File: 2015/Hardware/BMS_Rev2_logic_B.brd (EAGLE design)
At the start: 45.4 x 57.3 mm, 38 parts, among them Q9 MOSFET-NCHANNEL2N7002PW

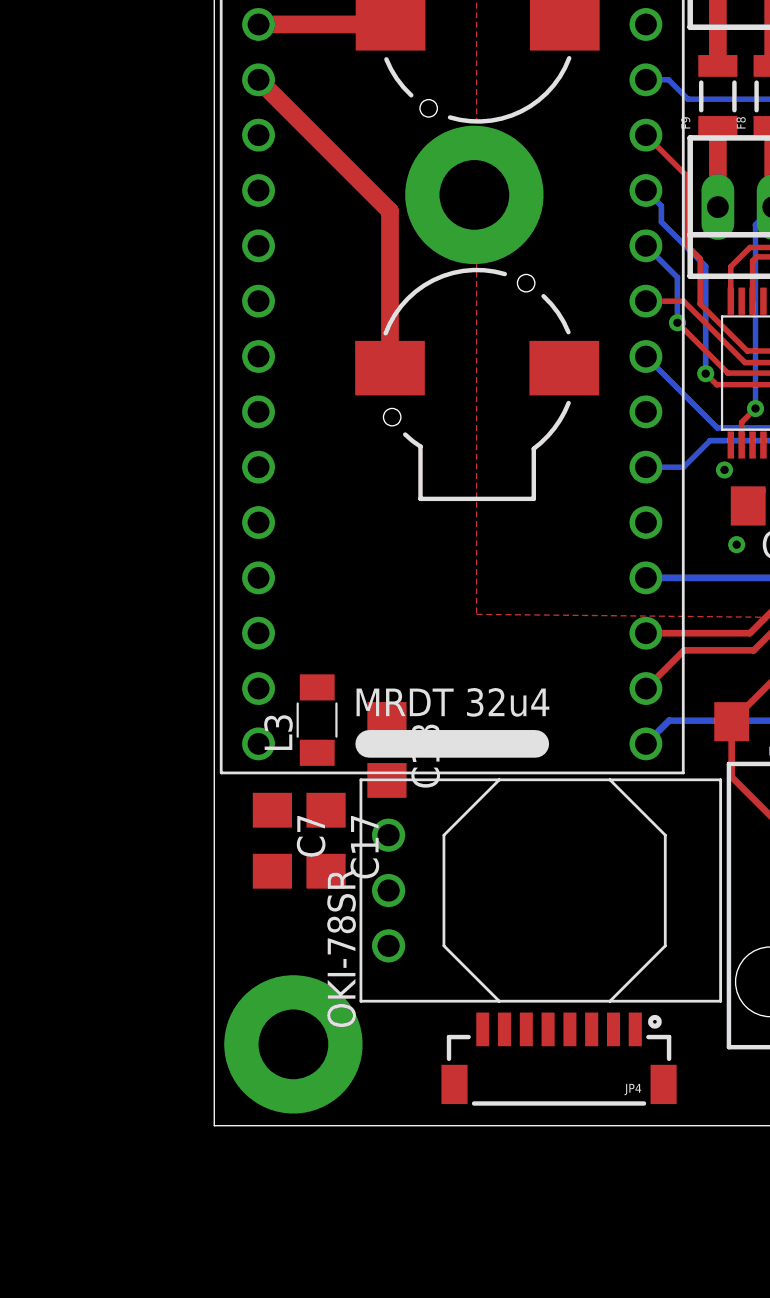
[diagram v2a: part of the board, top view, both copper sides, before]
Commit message: Completed the routing. Needs DRC Check and Clearance adjustments on the polygons
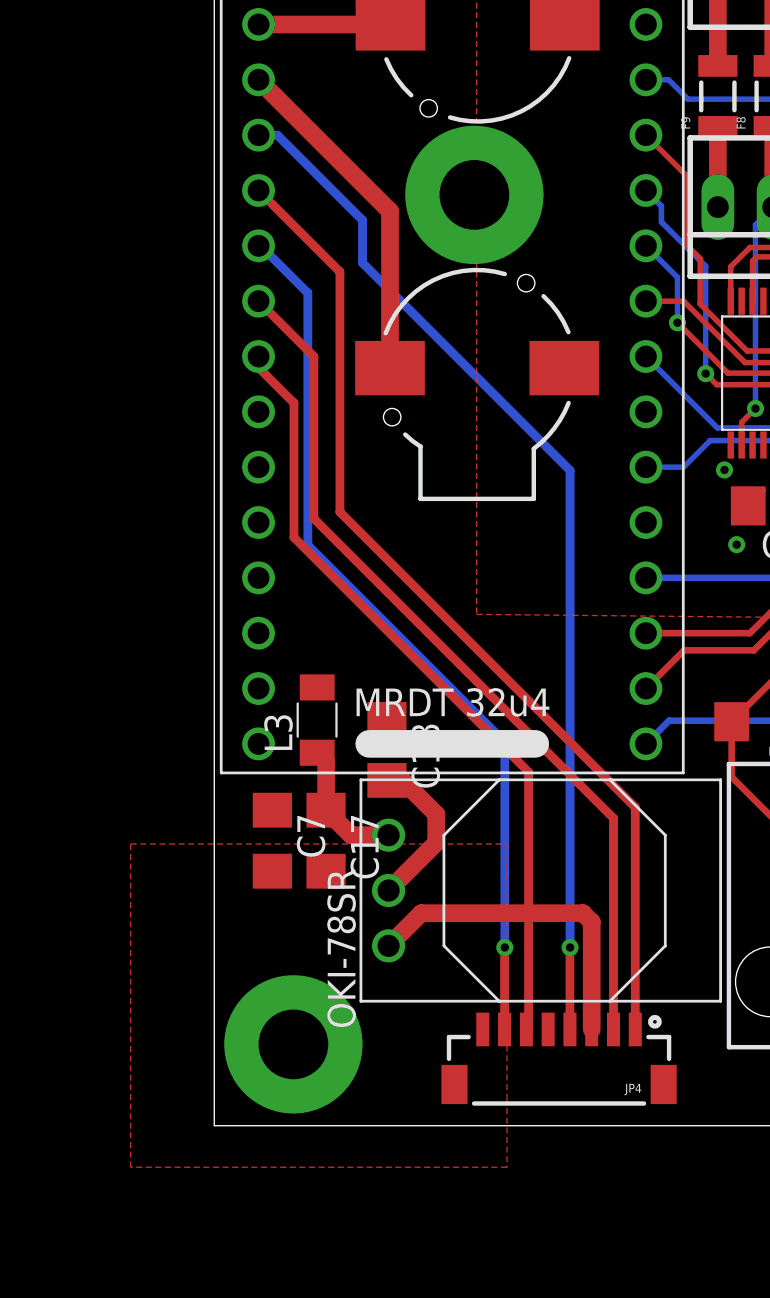
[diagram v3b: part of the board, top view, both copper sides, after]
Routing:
- net V_CHECK: track 0.00 -> 47.5 mm, vias 0 -> 1
- net V_CHG: track 0.00 -> 45.7 mm
- net V_OUT: track 0.00 -> 40.7 mm, vias 0 -> 1
- net I_ARRAY: track 0.00 -> 40.2 mm
- net GATE: track 0.00 -> 36.1 mm
- net LOGIC_POWER: track 0.00 -> 15.0 mm
- net GND: track 23.7 -> 31.0 mm
- net N$100: track 0.00 -> 6.15 mm
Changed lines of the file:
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@@
 <contactref element="S2" pad="P1"/>
 <contactref element="S3" pad="P1"/>
+<polygon width="0.8128" layer="1">
+<vertex x="-3.8354" y="9.6266"/>
+<vertex x="13.4366" y="9.6266"/>
+<vertex x="13.4366" y="-2.0574"/>
+<vertex x="13.4366" y="-5.207"/>
+<vertex x="-3.8354" y="-5.207"/>
+</polygon>
+<wire x1="7.9248" y1="12.5446" x2="8.639" y2="12.5446" width="0.8128" layer="1"/>
+<wire x1="8.639" y1="12.5446" x2="10.1854" y2="10.9982" width="0.8128" layer="1"/>
+<wire x1="10.1854" y1="10.9982" x2="10.1854" y2="9.6774" width="0.8128" layer="1"/>
+<wire x1="10.1854" y1="9.6774" x2="8.001" y2="7.493" width="0.8128" layer="1"/>
 <wire x1="25.206" y1="25.844" x2="25.206" y2="27.942" width="0" layer="19" extent="1-1"/>
-<wire x1="5.1308" y1="8.379" x2="8.001" y2="7.493" width="0" layer="19" extent="1-1"/>
-<wire x1="2.667" y1="8.379" x2="5.1308" y2="8.379" width="0" layer="19" extent="1-1"/>
-<wire x1="7.9248" y1="12.5446" x2="5.1308" y2="8.379" width="0" layer="19" extent="1-1"/>
-<wire x1="12.3242" y1="1.1176" x2="8.001" y2="7.493" width="0" layer="19" extent="1-1"/>
 </signal>
 <signal name="GATE">
 <contactref element="U$3" pad="25"/>
 <contactref element="JP4" pad="6"/>
-<wire x1="14.3242" y1="1.1176" x2="2.032" y2="32.004" width="0" layer="19" extent="1-1"/>
+<wire x1="14.3242" y1="1.1176" x2="14.4272" y2="1.2206" width="0.4064" layer="1"/>
+<wire x1="14.4272" y1="1.2206" x2="14.4272" y2="12.9286" width="0.4064" layer="1"/>
+<wire x1="14.4272" y1="12.9286" x2="3.6576" y2="23.6982" width="0.4064" layer="1"/>
+<wire x1="3.6576" y1="23.6982" x2="3.6576" y2="29.8704" width="0.4064" layer="1"/>
+<wire x1="3.6576" y1="29.8704" x2="2.032" y2="31.496" width="0.4064" layer="1"/>
+<wire x1="2.032" y1="31.496" x2="2.032" y2="32.004" width="0.4064" layer="1"/>
 </signal>
 <signal name="I_ARRAY">
 <contactref element="U$3" pad="24"/>
 <contactref element="JP4" pad="2"/>
-<wire x1="18.3242" y1="1.1176" x2="2.032" y2="34.544" width="0" layer="19" extent="1-1"/>
+<wire x1="18.3242" y1="1.1176" x2="18.3242" y2="10.8096" width="0.4064" layer="1"/>
+<wire x1="18.3242" y1="10.8096" x2="4.572" y2="24.5618" width="0.4064" layer="1"/>
+<wire x1="4.572" y1="24.5618" x2="4.572" y2="32.004" width="0.4064" layer="1"/>
+<wire x1="4.572" y1="32.004" x2="2.032" y2="34.544" width="0.4064" layer="1"/>
 </signal>
 <signal name="SDA">
@@
 <contactref element="L3" pad="1"/>
 <contactref element="OKI-78SR" pad="3"/>
-<wire x1="4.7244" y1="13.8162" x2="5.1308" y2="11.179" width="0" layer="19" extent="1-1"/>
-<wire x1="8.001" y1="10.033" x2="5.1308" y2="11.179" width="0" layer="19" extent="1-1"/>
+<wire x1="5.1308" y1="11.179" x2="5.1308" y2="13.4098" width="0.8128" layer="1"/>
+<wire x1="5.1308" y1="13.4098" x2="4.7244" y2="13.8162" width="0.8128" layer="1"/>
+<wire x1="8.001" y1="10.033" x2="6.2768" y2="10.033" width="0.8128" layer="1"/>
+<wire x1="6.2768" y1="10.033" x2="5.1308" y2="11.179" width="0.8128" layer="1"/>
 </signal>
 <signal name="RXD">
@@
 <contactref element="JP4" pad="7"/>
 <contactref element="U$3" pad="23"/>
-<wire x1="13.3242" y1="1.1176" x2="2.032" y2="37.084" width="0" layer="19" extent="1-1"/>
+<wire x1="2.032" y1="37.084" x2="2.1336" y2="37.084" width="0.4064" layer="16"/>
+<wire x1="2.1336" y1="37.084" x2="4.2926" y2="34.925" width="0.4064" layer="16"/>
+<wire x1="4.2926" y1="34.925" x2="4.2926" y2="23.3426" width="0.4064" layer="16"/>
+<wire x1="4.2926" y1="23.3426" x2="13.335" y2="14.3002" width="0.4064" layer="16"/>
+<wire x1="13.335" y1="14.3002" x2="13.335" y2="4.8768" width="0.4064" layer="16"/>
+<via x="13.335" y="4.8768" extent="1-16" drill="0.381"/>
+<wire x1="13.335" y1="4.8768" x2="13.3242" y2="4.866" width="0.4064" layer="1"/>
+<wire x1="13.3242" y1="4.866" x2="13.3242" y2="1.1176" width="0.4064" layer="1"/>
 </signal>
 <signal name="V_CHECK">
 <contactref element="JP4" pad="4"/>
 <contactref element="U$3" pad="21"/>
-<wire x1="16.3242" y1="1.1176" x2="2.032" y2="42.164" width="0" layer="19" extent="1-1"/>
+<wire x1="2.032" y1="42.164" x2="2.8956" y2="42.164" width="0.4064" layer="16"/>
+<wire x1="2.8956" y1="42.164" x2="6.8072" y2="38.2524" width="0.4064" layer="16"/>
+<wire x1="6.8072" y1="38.2524" x2="6.8072" y2="36.2966" width="0.4064" layer="16"/>
+<wire x1="6.8072" y1="36.2966" x2="16.3322" y2="26.7716" width="0.4064" layer="16"/>
+<wire x1="16.3322" y1="26.7716" x2="16.3322" y2="4.8768" width="0.4064" layer="16"/>
+<via x="16.3322" y="4.8768" extent="1-16" drill="0.381"/>
+<wire x1="16.3322" y1="4.8768" x2="16.3242" y2="4.8688" width="0.4064" layer="1"/>
+<wire x1="16.3242" y1="4.8688" x2="16.3242" y2="1.1176" width="0.4064" layer="1"/>
 </signal>
 <signal name="V_CHG">
 <contactref element="JP4" pad="1"/>
 <contactref element="U$3" pad="22"/>
-<wire x1="19.3242" y1="1.1176" x2="2.032" y2="39.624" width="0" layer="19" extent="1-1"/>
+<wire x1="19.3242" y1="1.1176" x2="19.3242" y2="11.3082" width="0.4064" layer="1"/>
+<wire x1="19.3242" y1="11.3082" x2="5.7658" y2="24.8666" width="0.4064" layer="1"/>
+<wire x1="5.7658" y1="24.8666" x2="5.7658" y2="35.8902" width="0.4064" layer="1"/>
+<wire x1="5.7658" y1="35.8902" x2="2.032" y2="39.624" width="0.4064" layer="1"/>
 </signal>
 <signal name="LOGIC_POWER">
 <contactref element="JP4" pad="3"/>
 <contactref element="OKI-78SR" pad="1"/>
-<wire x1="8.001" y1="4.953" x2="17.3242" y2="1.1176" width="0" layer="19" extent="1-1"/>
+<wire x1="17.3242" y1="1.1176" x2="17.3242" y2="6.0438" width="0.8128" layer="1"/>
+<wire x1="17.3242" y1="6.0438" x2="16.9164" y2="6.4516" width="0.8128" layer="1"/>
+<wire x1="16.9164" y1="6.4516" x2="9.4996" y2="6.4516" width="0.8128" layer="1"/>
+<wire x1="9.4996" y1="6.4516" x2="8.001" y2="4.953" width="0.8128" layer="1"/>
 </signal>
 <signal name="N$4">

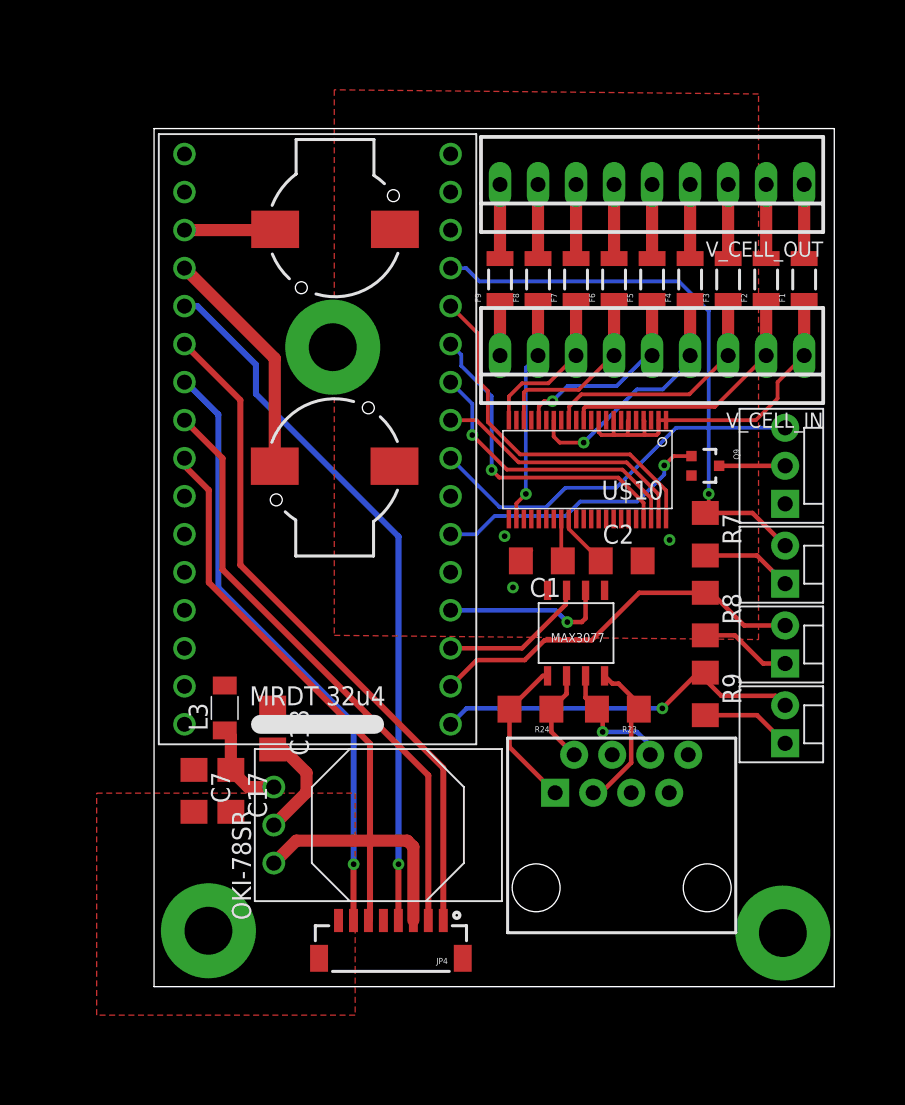
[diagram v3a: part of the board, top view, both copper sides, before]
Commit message: Added Polygons and cleaned up traces. Still clearancework  needs to be done.
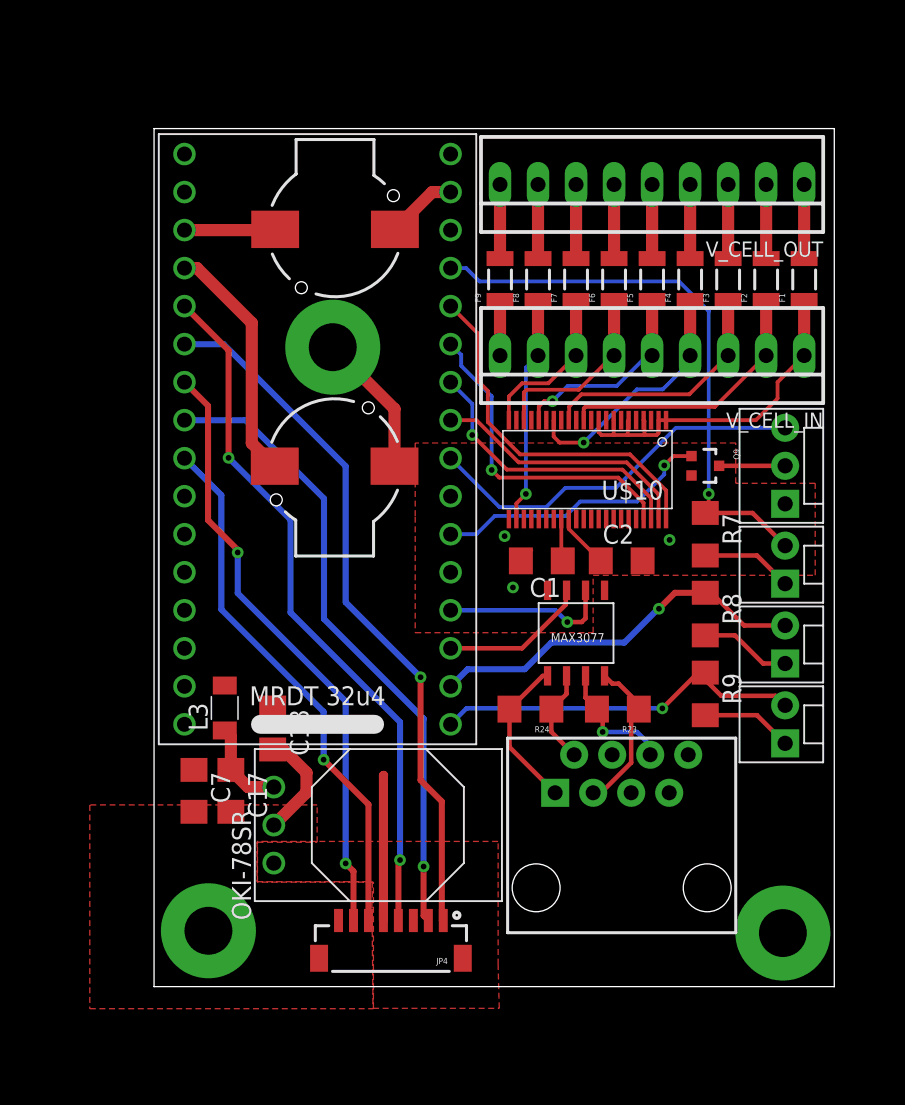
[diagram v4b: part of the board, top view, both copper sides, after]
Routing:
- net LOGIC_POWER: track 15.0 -> 0.00 mm
- net GND: track 31.0 -> 45.4 mm
- net 5V: track 0.00 -> 9.71 mm
- net I_ARRAY: track 40.2 -> 42.6 mm, vias 0 -> 1
- net V_CHG: track 45.7 -> 47.3 mm, vias 0 -> 1
- net V_CHECK: track 47.5 -> 47.1 mm, vias 1 -> 2
- net GATE: track 36.1 -> 36.0 mm, vias 0 -> 1
- net V_OUT: track 40.7 -> 40.6 mm, vias 1 -> 2
- net SW_LCDWAKE: vias 0 -> 1
- added copper zone on layer 1, net LOGIC_POWER
